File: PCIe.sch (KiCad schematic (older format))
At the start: 17 parts, among them J2 Bus_PCI_Express_Mini, U1 IMX8MM

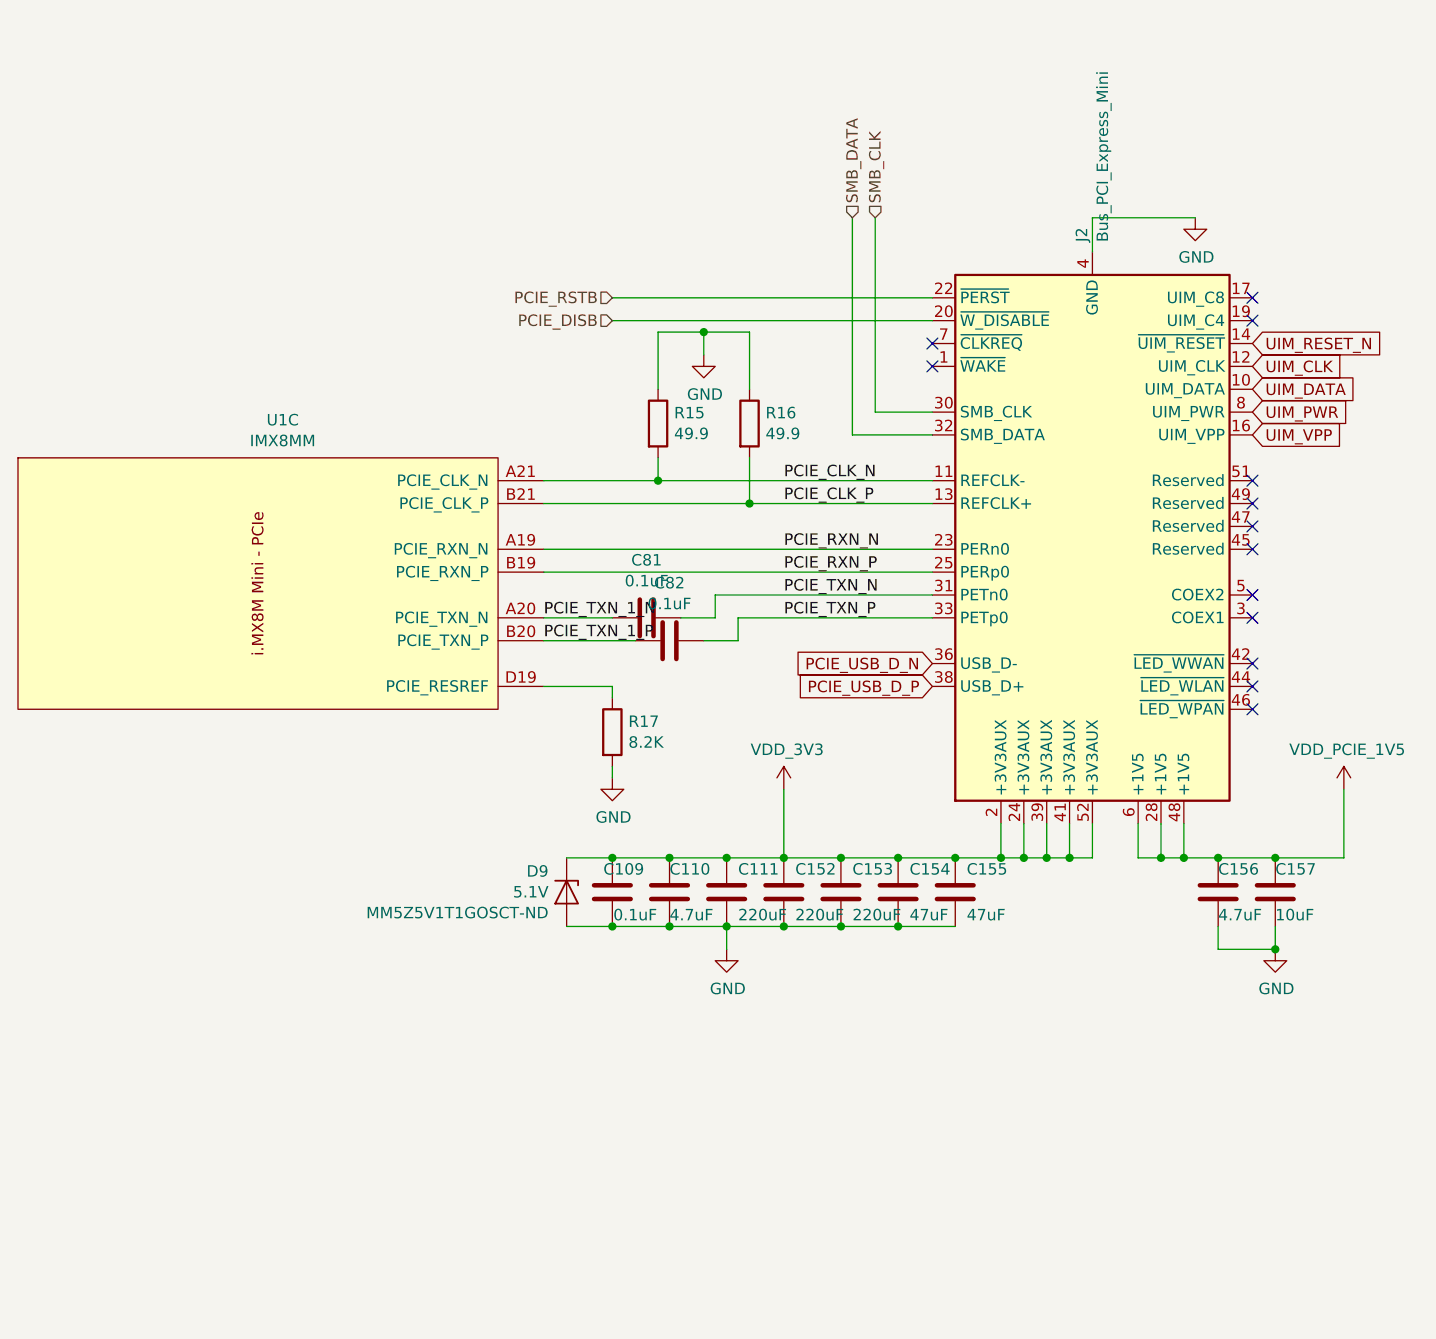
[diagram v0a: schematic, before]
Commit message: Re-annotate schematics, add dnp field, and silkscreen cleanup
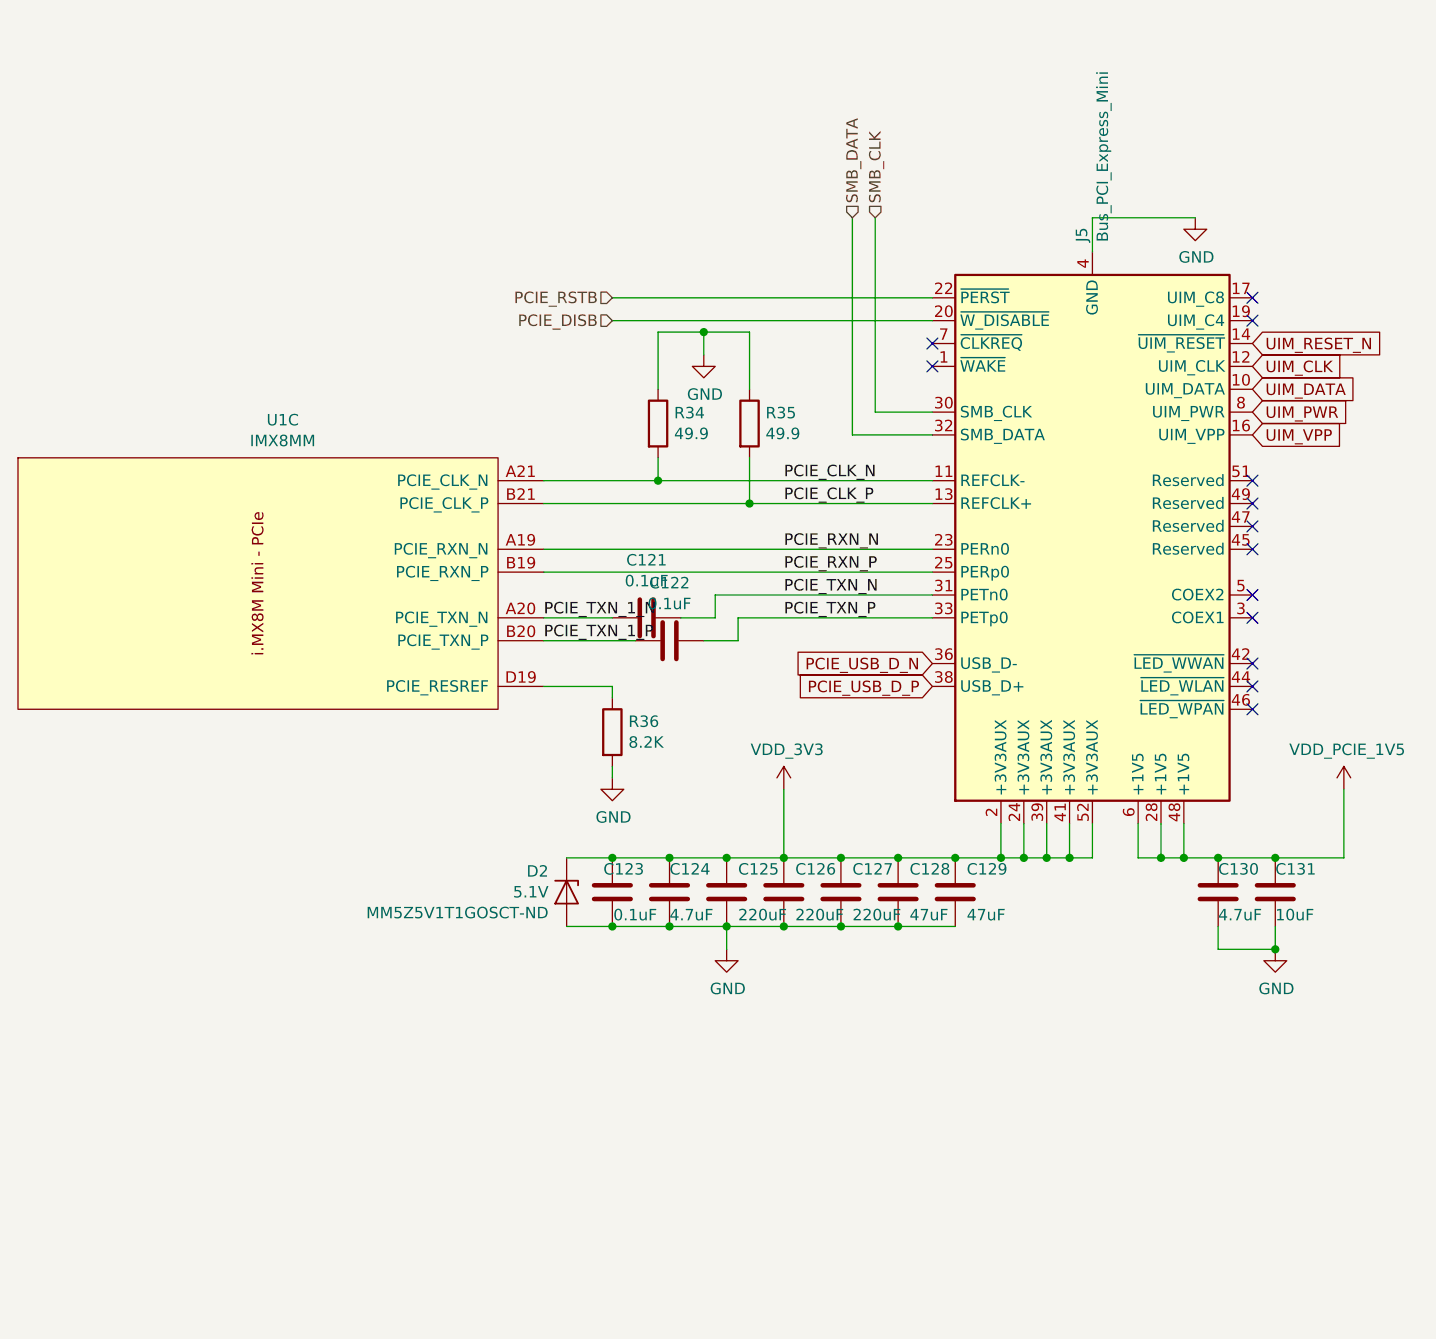
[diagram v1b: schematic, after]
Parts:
- renumbered C81 to C121, C82 to C122, C109 to C123, C110 to C124, C111 to C125, C152 to C126, C153 to C127, C154 to C128, C155 to C129, C156 to C130, C157 to C131, D9 to D2, J2 to J5, R15 to R34, R16 to R35, R17 to R36
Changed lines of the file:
@@
 P 7350 3750
 AR Path="/5D31B8E0" Ref="J?"  Part="1"
-AR Path="/5D31363C/5D31B8E0" Ref="J2"  Part="1"
-F 0 "J2" V 7304 2506 50  0000 R CNN
+AR Path="/5D31363C/5D31B8E0" Ref="J5"  Part="1"
+F 0 "J5" V 7304 2506 50  0000 R CNN
 F 1 "Bus_PCI_Express_Mini" V 7395 2506 50  0000 R CNN
 F 2 "mxenc:1775838-2-NPTH" H 7350 3750 50  0001 C CNN
@@
 $EndComp
 $Comp
-L Device:R R17
+L Device:R R36
 U 1 1 5D33A08E
 P 5250 4650
-F 0 "R17" H 5320 4696 50  0000 L CNN
+F 0 "R36" H 5320 4696 50  0000 L CNN
 F 1 "8.2K" H 5320 4605 50  0000 L CNN
 F 2 "Resistor_SMD:R_0201_0603Metric" V 5180 4650 50  0001 C CNN
@@
 	5250 4450 4950 4450
 $Comp
-L power:GND #PWR0148
+L power:GND #PWR0133
 U 1 1 5D33B223
 P 5250 4850
-F 0 "#PWR0148" H 5250 4600 50  0001 C CNN
+F 0 "#PWR0133" H 5250 4600 50  0001 C CNN
 F 1 "GND" H 5255 4677 50  0000 C CNN
 F 2 "" H 5250 4850 50  0001 C CNN
@@
 	5800 4250 5800 4150
 $Comp
-L Device:R R15
+L Device:R R34
 U 1 1 5D34706E
 P 5450 3300
-F 0 "R15" H 5520 3346 50  0000 L CNN
+F 0 "R34" H 5520 3346 50  0000 L CNN
 F 1 "49.9" H 5520 3255 50  0000 L CNN
 F 2 "Resistor_SMD:R_0201_0603Metric" V 5380 3300 50  0001 C CNN
@@
 $EndComp
 $Comp
-L Device:R R16
+L Device:R R35
 U 1 1 5D347D6E
 P 5850 3300
-F 0 "R16" H 5920 3346 50  0000 L CNN
+F 0 "R35" H 5920 3346 50  0000 L CNN
 F 1 "49.9" H 5920 3255 50  0000 L CNN
 F 2 "Resistor_SMD:R_0201_0603Metric" V 5780 3300 50  0001 C CNN
@@
 	5850 3650 4950 3650
 $Comp
-L power:GND #PWR0149
+L power:GND #PWR0132
 U 1 1 5D34AF2E
 P 5650 3000
-F 0 "#PWR0149" H 5650 2750 50  0001 C CNN
+F 0 "#PWR0132" H 5650 2750 50  0001 C CNN
 F 1 "GND" H 5655 2827 50  0000 C CNN
 F 2 "" H 5650 3000 50  0001 C CNN
@@
 Connection ~ 5650 2900
 $Comp
-L mxenc:VDD_3V3 #PWR0172
+L mxenc:VDD_3V3 #PWR0134
 U 1 1 5D62C02A
 P 6000 4900
-F 0 "#PWR0172" H 6000 4750 50  0001 C CNN
+F 0 "#PWR0134" H 6000 4750 50  0001 C CNN
 F 1 "VDD_3V3" H 6015 5073 50  0000 C CNN
 F 2 "" H 6000 4900 50  0001 C CNN
@@
 	7750 5200 7650 5200
 $Comp
-L mxenc:VDD_PCIE_1V5 #PWR0180
+L mxenc:VDD_PCIE_1V5 #PWR0135
 U 1 1 5D650001
 P 8450 4900
-F 0 "#PWR0180" H 8450 4750 50  0001 C CNN
+F 0 "#PWR0135" H 8450 4750 50  0001 C CNN
 F 1 "VDD_PCIE_1V5" H 8465 5073 50  0000 C CNN
 F 2 "" H 8450 4900 50  0001 C CNN
@@
 P 7900 5350
 AR Path="/5D1DA4BE/5D6B4E4C" Ref="C?"  Part="1"
-AR Path="/5D31363C/5D6B4E4C" Ref="C156"  Part="1"
-F 0 "C156" H 7900 5450 50  0000 L CNN
+AR Path="/5D31363C/5D6B4E4C" Ref="C130"  Part="1"
+F 0 "C130" H 7900 5450 50  0000 L CNN
 F 1 "4.7uF" H 7900 5250 50  0000 L CNN
 F 2 "Capacitor_SMD:C_0402_1005Metric" H 7938 5200 50  0001 C CNN
@@
 P 8150 5350
 AR Path="/5D1DA4BE/5D6C4737" Ref="C?"  Part="1"
-AR Path="/5D31363C/5D6C4737" Ref="C157"  Part="1"
-F 0 "C157" H 8150 5450 50  0000 L CNN
+AR Path="/5D31363C/5D6C4737" Ref="C131"  Part="1"
+F 0 "C131" H 8150 5450 50  0000 L CNN
 F 1 "10uF" H 8150 5250 50  0000 L CNN
 F 2 "Capacitor_SMD:C_0402_1005Metric" H 8188 5200 50  0001 C CNN
@@
 	8150 5200 8450 5200
 $Comp
-L Device:C C155
+L Device:C C129
 U 1 1 5D6CB0D7
 P 6750 5350
-F 0 "C155" H 6800 5450 50  0000 L CNN
+F 0 "C129" H 6800 5450 50  0000 L CNN
 F 1 "47uF" H 6800 5250 50  0000 L CNN
 F 2 "Capacitor_SMD:C_0805_2012Metric" H 6788 5200 50  0001 C CNN
@@
 	6750 5200 6950 5200
 $Comp
-L Device:C C154
+L Device:C C128
 U 1 1 5D6CBC0F
 P 6500 5350
-F 0 "C154" H 6550 5450 50  0000 L CNN
+F 0 "C128" H 6550 5450 50  0000 L CNN
 F 1 "47uF" H 6550 5250 50  0000 L CNN
 F 2 "Capacitor_SMD:C_0805_2012Metric" H 6538 5200 50  0001 C CNN
@@
 	6500 5200 6750 5200
 $Comp
-L Device:C C153
+L Device:C C127
 U 1 1 5D6CBE84
 P 6250 5350
-F 0 "C153" H 6300 5450 50  0000 L CNN
+F 0 "C127" H 6300 5450 50  0000 L CNN
 F 1 "220uF" H 6300 5250 50  0000 L CNN
 F 2 "Capacitor_SMD:C_1206_3216Metric" H 6288 5200 50  0001 C CNN
@@
 	6250 5200 6500 5200
 $Comp
-L Device:C C152
+L Device:C C126
 U 1 1 5D6CC1DF
 P 6000 5350
-F 0 "C152" H 6050 5450 50  0000 L CNN
+F 0 "C126" H 6050 5450 50  0000 L CNN
 F 1 "220uF" H 6050 5250 50  0000 L CNN
 F 2 "Capacitor_SMD:C_1206_3216Metric" H 6038 5200 50  0001 C CNN
@@
 Connection ~ 6000 5200
 $Comp
-L Device:C C111
+L Device:C C125
 U 1 1 5D6CC566
 P 5750 5350
-F 0 "C111" H 5800 5450 50  0000 L CNN
+F 0 "C125" H 5800 5450 50  0000 L CNN
 F 1 "220uF" H 5800 5250 50  0000 L CNN
 F 2 "Capacitor_SMD:C_1206_3216Metric" H 5788 5200 50  0001 C CNN
@@
 	6000 5200 5750 5200
 $Comp
-L power:GND #PWR0195
+L power:GND #PWR0136
 U 1 1 5D6CDB4B
 P 5750 5600
-F 0 "#PWR0195" H 5750 5350 50  0001 C CNN
+F 0 "#PWR0136" H 5750 5350 50  0001 C CNN
 F 1 "GND" H 5755 5427 50  0000 C CNN
 F 2 "" H 5750 5600 50  0001 C CNN
@@
 P 5500 5350
 AR Path="/5D1DA4BE/5D6D4B0E" Ref="C?"  Part="1"
-AR Path="/5D31363C/5D6D4B0E" Ref="C110"  Part="1"
-F 0 "C110" H 5500 5450 50  0000 L CNN
+AR Path="/5D31363C/5D6D4B0E" Ref="C124"  Part="1"
+F 0 "C124" H 5500 5450 50  0000 L CNN
 F 1 "4.7uF" H 5500 5250 50  0000 L CNN
 F 2 "Capacitor_SMD:C_0402_1005Metric" H 5538 5200 50  0001 C CNN
@@
 	5500 5500 5750 5500
 $Comp
-L Device:C C109
+L Device:C C123
 U 1 1 5D6DCC3C
 P 5250 5350
-F 0 "C109" H 5300 5450 50  0000 C CNN
+F 0 "C123" H 5300 5450 50  0000 C CNN
 F 1 "0.1uF" H 5350 5250 50  0000 C CNN
 F 2 "Capacitor_SMD:C_0201_0603Metric" H 5288 5200 50  0001 C CNN
@@
 Connection ~ 5500 5500
 $Comp
-L Device:C C82
+L Device:C C122
 U 1 1 5D342B0F
 P 5500 4250
-F 0 "C82" V 5248 4250 50  0000 C CNN
+F 0 "C122" V 5248 4250 50  0000 C CNN
 F 1 "0.1uF" V 5339 4250 50  0000 C CNN
 F 2 "Capacitor_SMD:C_0201_0603Metric" H 5538 4100 50  0001 C CNN
@@
 	6300 3350 6300 2400
 $Comp
-L power:GND #PWR0197
+L power:GND #PWR0131
 U 1 1 5D7014D5
 P 7800 2400
-F 0 "#PWR0197" H 7800 2150 50  0001 C CNN
+F 0 "#PWR0131" H 7800 2150 50  0001 C CNN
 F 1 "GND" H 7805 2227 50  0000 C CNN
 F 2 "" H 7800 2400 50  0001 C CNN
@@
 NoConn ~ 6650 3050
 $Comp
-L power:GND #PWR0198
+L power:GND #PWR0137
 U 1 1 5D779D7D
 P 8150 5600
-F 0 "#PWR0198" H 8150 5350 50  0001 C CNN
+F 0 "#PWR0137" H 8150 5350 50  0001 C CNN
 F 1 "GND" H 8155 5427 50  0000 C CNN
 F 2 "" H 8150 5600 50  0001 C CNN
@@
 	5700 4150 5550 4150
 $Comp
-L Device:C C81
+L Device:C C121
 U 1 1 5D34369A
 P 5400 4150
-F 0 "C81" V 5148 4150 50  0000 C CNN
+F 0 "C121" V 5148 4150 50  0000 C CNN
 F 1 "0.1uF" V 5239 4150 50  0000 C CNN
 F 2 "Capacitor_SMD:C_0201_0603Metric" H 5438 4000 50  0001 C CNN
@@
 PCIE_USB_D_P
 $Comp
-L Device:D_Zener D9
+L Device:D_Zener D2
 U 1 1 5ECE4766
 P 5050 5350
-F 0 "D9" V 4959 5271 50  0000 R CNN
+F 0 "D2" V 4959 5271 50  0000 R CNN
 F 1 "5.1V" V 5050 5271 50  0000 R CNN
 F 2 "Diode_SMD:D_SOD-523" H 5050 5350 50  0001 C CNN

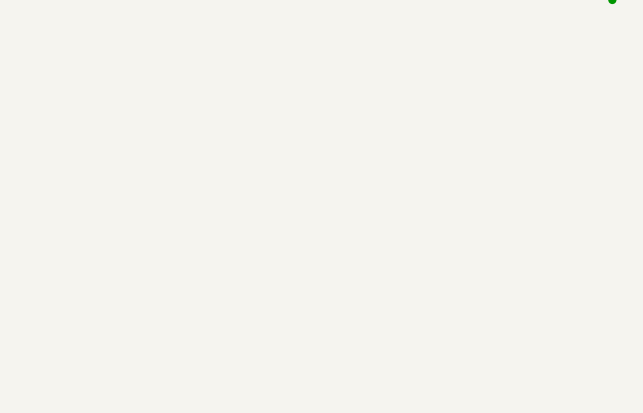
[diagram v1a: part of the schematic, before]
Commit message: Split mounting holes from pcie and put them on the front side
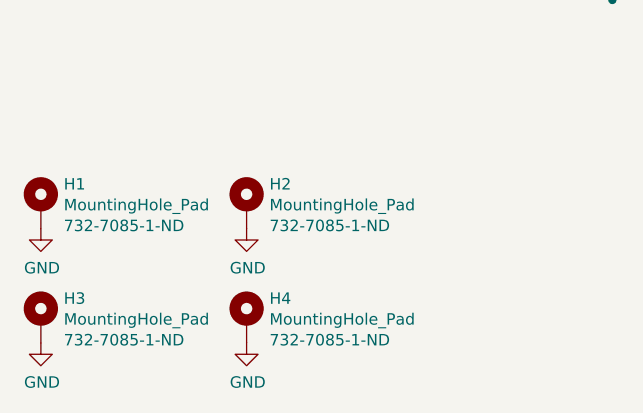
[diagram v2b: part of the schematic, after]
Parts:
- added H1, H2, H3, H4: MountingHole_Pad, mxenc:MountingHole_M2_Standoff, symbol Mechanical:MountingHole_Pad
- J5: footprint mxenc:1775838-2-NPTH -> mxenc:1775838-2_conn_only
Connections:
- net GND: now also H1.1, H2.1, H3.1, H4.1
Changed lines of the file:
@@
 F 0 "J5" V 7304 2506 50  0000 R CNN
 F 1 "Bus_PCI_Express_Mini" V 7395 2506 50  0000 R CNN
-F 2 "mxenc:1775838-2-NPTH" H 7350 3750 50  0001 C CNN
+F 2 "mxenc:1775838-2_conn_only" H 7350 3750 50  0001 C CNN
 F 3 "~" H 7200 2600 50  0001 C CNN
 F 4 "TE" H 7350 3750 50  0001 C CNN "Mfgr"
@@
 	5050 5500 5250 5500
 Connection ~ 5250 5500
+$Comp
+L Mechanical:MountingHole_Pad H1
+U 1 1 5EF33699
+P 2750 6400
+F 0 "H1" H 2850 6494 50  0000 L CNN
+F 1 "MountingHole_Pad" H 2850 6403 50  0000 L CNN
+F 2 "mxenc:MountingHole_M2_Standoff" H 2750 6400 50  0001 C CNN
+F 3 "~" H 2750 6400 50  0001 C CNN
+F 4 "732-7085-1-ND" H 2850 6312 50  0000 L CNN "Vendorpart"
+F 5 "Wurth" H 2750 6400 50  0001 C CNN "Mfgr"
+F 6 "9774030243R" H 2750 6400 50  0001 C CNN "Part"
+	1    2750 6400
+	1    0    0    -1
+$EndComp
+$Comp
+L power:GND #PWR0224
+U 1 1 5EF36759
+P 2750 6500
+F 0 "#PWR0224" H 2750 6250 50  0001 C CNN
+F 1 "GND" H 2755 6327 50  0000 C CNN
+F 2 "" H 2750 6500 50  0001 C CNN
+F 3 "" H 2750 6500 50  0001 C CNN
+	1    2750 6500
+	1    0    0    -1
+$EndComp
+$Comp
+L power:GND #PWR0225
+U 1 1 5EF36E95
+P 3650 6500
+F 0 "#PWR0225" H 3650 6250 50  0001 C CNN
+F 1 "GND" H 3655 6327 50  0000 C CNN
+F 2 "" H 3650 6500 50  0001 C CNN
+F 3 "" H 3650 6500 50  0001 C CNN
+	1    3650 6500
+	1    0    0    -1
+$EndComp
+$Comp
+L power:GND #PWR0226
+U 1 1 5EF371F7
+P 2750 7000
+F 0 "#PWR0226" H 2750 6750 50  0001 C CNN
+F 1 "GND" H 2755 6827 50  0000 C CNN
+F 2 "" H 2750 7000 50  0001 C CNN
+F 3 "" H 2750 7000 50  0001 C CNN
+	1    2750 7000
+	1    0    0    -1
+$EndComp
+$Comp
+L power:GND #PWR0227
+U 1 1 5EF376AD
+P 3650 7000
+F 0 "#PWR0227" H 3650 6750 50  0001 C CNN
+F 1 "GND" H 3655 6827 50  0000 C CNN
+F 2 "" H 3650 7000 50  0001 C CNN
+F 3 "" H 3650 7000 50  0001 C CNN
+	1    3650 7000
+	1    0    0    -1
+$EndComp
+$Comp
+L Mechanical:MountingHole_Pad H2
+U 1 1 5EF4EB1A
+P 3650 6400
+F 0 "H2" H 3750 6494 50  0000 L CNN
+F 1 "MountingHole_Pad" H 3750 6403 50  0000 L CNN
+F 2 "mxenc:MountingHole_M2_Standoff" H 3650 6400 50  0001 C CNN
+F 3 "~" H 3650 6400 50  0001 C CNN
+F 4 "732-7085-1-ND" H 3750 6312 50  0000 L CNN "Vendorpart"
+F 5 "Wurth" H 3650 6400 50  0001 C CNN "Mfgr"
+F 6 "9774030243R" H 3650 6400 50  0001 C CNN "Part"
+	1    3650 6400
+	1    0    0    -1
+$EndComp
+$Comp
+L Mechanical:MountingHole_Pad H4
+U 1 1 5EF4F011
+P 3650 6900
+F 0 "H4" H 3750 6994 50  0000 L CNN
+F 1 "MountingHole_Pad" H 3750 6903 50  0000 L CNN
+F 2 "mxenc:MountingHole_M2_Standoff" H 3650 6900 50  0001 C CNN
+F 3 "~" H 3650 6900 50  0001 C CNN
+F 4 "732-7085-1-ND" H 3750 6812 50  0000 L CNN "Vendorpart"
+F 5 "Wurth" H 3650 6900 50  0001 C CNN "Mfgr"
+F 6 "9774030243R" H 3650 6900 50  0001 C CNN "Part"
+	1    3650 6900
+	1    0    0    -1
+$EndComp
+$Comp
+L Mechanical:MountingHole_Pad H3
+U 1 1 5EF4F2A0
+P 2750 6900
+F 0 "H3" H 2850 6994 50  0000 L CNN
+F 1 "MountingHole_Pad" H 2850 6903 50  0000 L CNN
+F 2 "mxenc:MountingHole_M2_Standoff" H 2750 6900 50  0001 C CNN
+F 3 "~" H 2750 6900 50  0001 C CNN
+F 4 "732-7085-1-ND" H 2850 6812 50  0000 L CNN "Vendorpart"
+F 5 "Wurth" H 2750 6900 50  0001 C CNN "Mfgr"
+F 6 "9774030243R" H 2750 6900 50  0001 C CNN "Part"
+	1    2750 6900
+	1    0    0    -1
+$EndComp
 $EndSCHEMATC
